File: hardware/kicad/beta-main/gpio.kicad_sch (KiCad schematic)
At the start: 1 part

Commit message: tweaks and added servo controller
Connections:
- net UART3_TX: now reaches Module1.39 (GPIO8)
- net UART3_RX: now reaches Module1.40 (GPIO9)
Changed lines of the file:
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@@
+	(wire
+		(pts
+			(xy 129.54 92.71) (xy 140.97 92.71)
+		)
+		(stroke
+			(width 0)
+			(type default)
+		)
+	)
 	(wire
 		(pts
@@
 		(pts
 			(xy 130.81 148.59) (xy 130.81 146.05)
+		)
+		(stroke
+			(width 0)
+			(type default)
+		)
+	)
+	(wire
+		(pts
+			(xy 57.15 92.71) (xy 68.58 92.71)
 		)
 		(stroke
@@
 		)
 	)
+	(hierarchical_label "UART3_TX"
+		(shape passive)
+		(at 140.97 92.71 0)
+		(effects
+			(font
+				(size 1.27 1.27)
+			)
+			(justify left)
+		)
+	)
 	(hierarchical_label "GND"
 		(shape passive)
@@
 		(effects
 			(font
+				(size 1.27 1.27)
+			)
+			(justify right)
+		)
+	)
+	(hierarchical_label "UART3_RX"
+		(shape passive)
+		(at 57.15 92.71 180)
+		(effects
+			(font

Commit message: tweaks
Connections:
- net CAM_GPIO1: now reaches Module1.100 (CAM_GPIO1)
- net CAM_GPIO0: now reaches Module1.97 (CAM_GPIO0)
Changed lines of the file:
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@@
+	(wire
+		(pts
+			(xy 62.23 168.91) (xy 68.58 168.91)
+		)
+		(stroke
+			(width 0)
+			(type default)
+		)
+	)
 	(wire
 		(pts
@@
 	(wire
 		(pts
+			(xy 129.54 166.37) (xy 134.62 166.37)
+		)
+		(stroke
+			(width 0)
+			(type default)
+		)
+	)
+	(wire
+		(pts
 			(xy 66.04 69.85) (xy 68.58 69.85)
 		)
@@
 		(shape passive)
 		(at 66.04 95.25 180)
+		(effects
+			(font
+				(size 1.27 1.27)
+			)
+			(justify right)
+		)
+	)
+	(hierarchical_label "SDA1"
+		(shape passive)
+		(at 22.86 128.27 180)
 		(effects
 			(font
@@
 		)
 	)
+	(hierarchical_label "CAM_GPIO0"
+		(shape input)
+		(at 134.62 166.37 0)
+		(effects
+			(font
+				(size 1.27 1.27)
+			)
+			(justify left)
+		)
+	)
 	(hierarchical_label "GND"
 		(shape passive)
@@
 		)
 	)
+	(hierarchical_label "SCL1"
+		(shape passive)
+		(at 22.86 124.46 180)
+		(effects
+			(font
+				(size 1.27 1.27)
+			)
+			(justify right)
+		)
+	)
 	(hierarchical_label "UART3_TX"
 		(shape passive)
@@
 		)
 	)
+	(hierarchical_label "CAM_GPIO1"
+		(shape input)
+		(at 62.23 168.91 180)
+		(effects
+			(font
+				(size 1.27 1.27)
+			)
+			(justify right)
+		)
+	)

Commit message: Wzmacniacz dodany
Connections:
- net GPIO21: now reaches Module1.25 (GPIO21)
- net GPIO19: now reaches Module1.26 (GPIO19)
- net GPIO18: now reaches Module1.49 (GPIO18)
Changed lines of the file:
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@@
+		)
+	)
+	(hierarchical_label "GPIO21"
+		(shape input)
+		(at 129.54 74.93 0)
+		(effects
+			(font
+				(size 1.27 1.27)
+			)
+			(justify left)
 		)
 	)
@@
 		(effects
 			(font
+				(size 1.27 1.27)
+			)
+			(justify left)
+		)
+	)
+	(hierarchical_label "GPIO19"
+		(shape input)
+		(at 68.58 74.93 180)
+		(effects
+			(font
+				(size 1.27 1.27)
+			)
+			(justify right)
+		)
+	)
+	(hierarchical_label "GPIO18"
+		(shape input)
+		(at 129.54 105.41 0)
+		(effects
+			(font

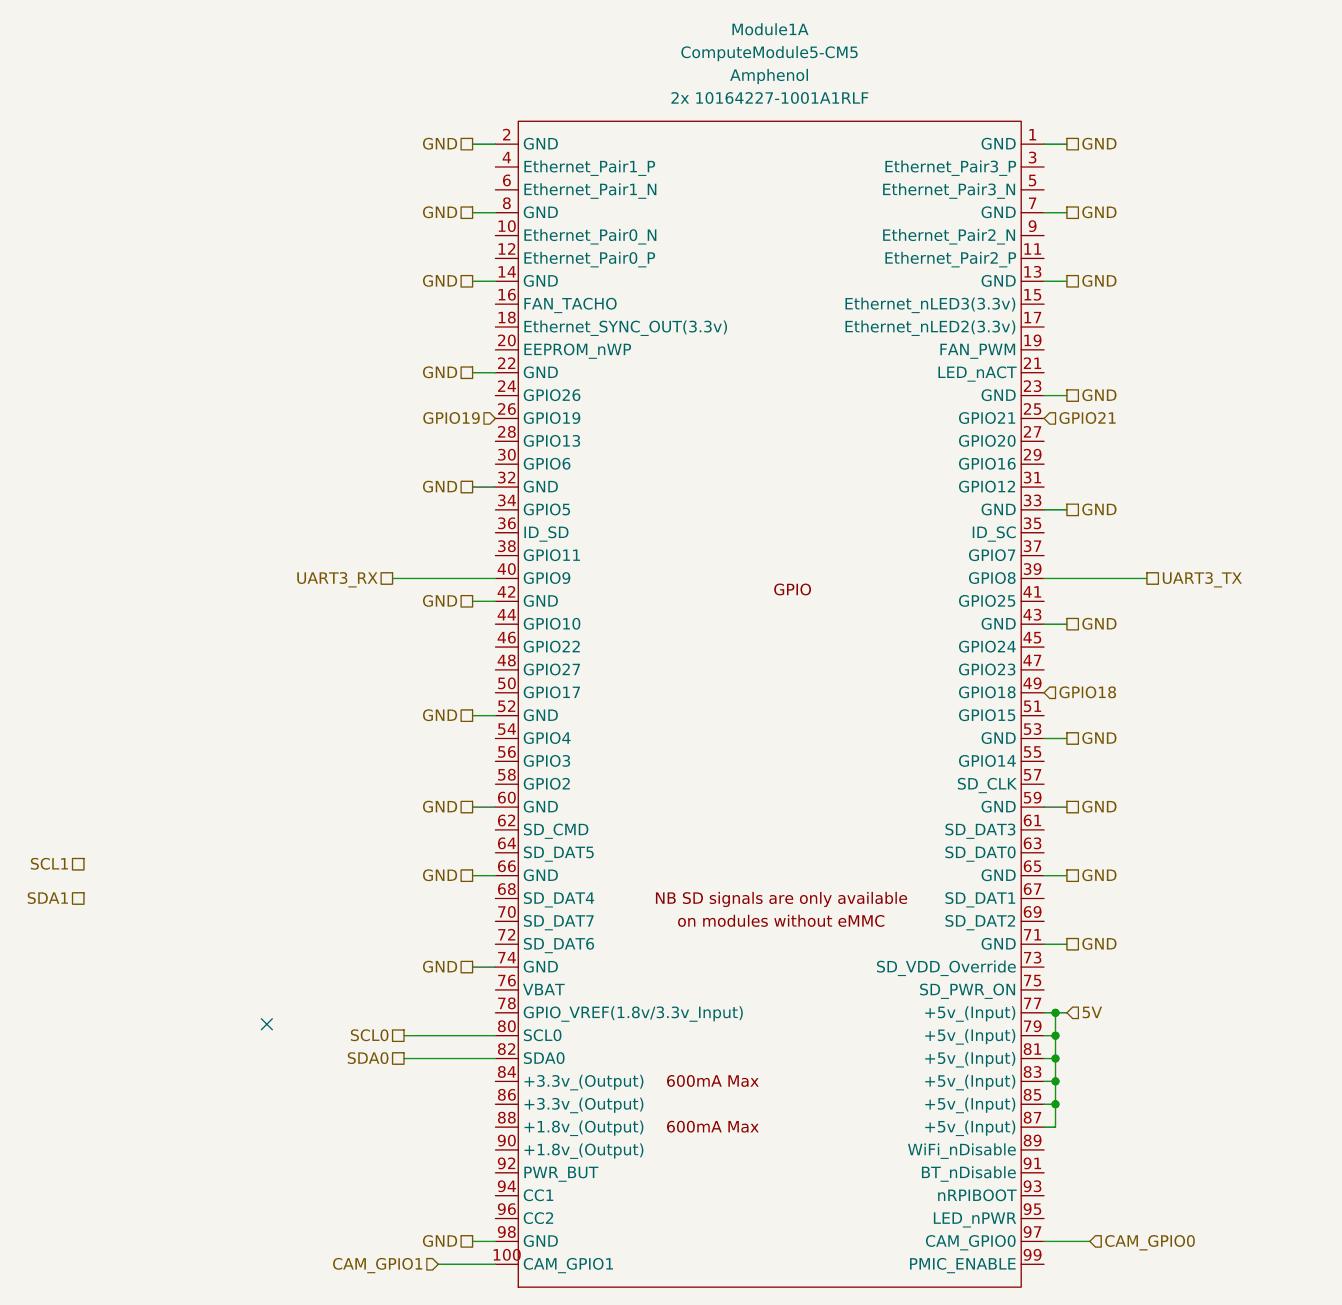
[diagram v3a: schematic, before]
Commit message: 5V and amplifier corrections
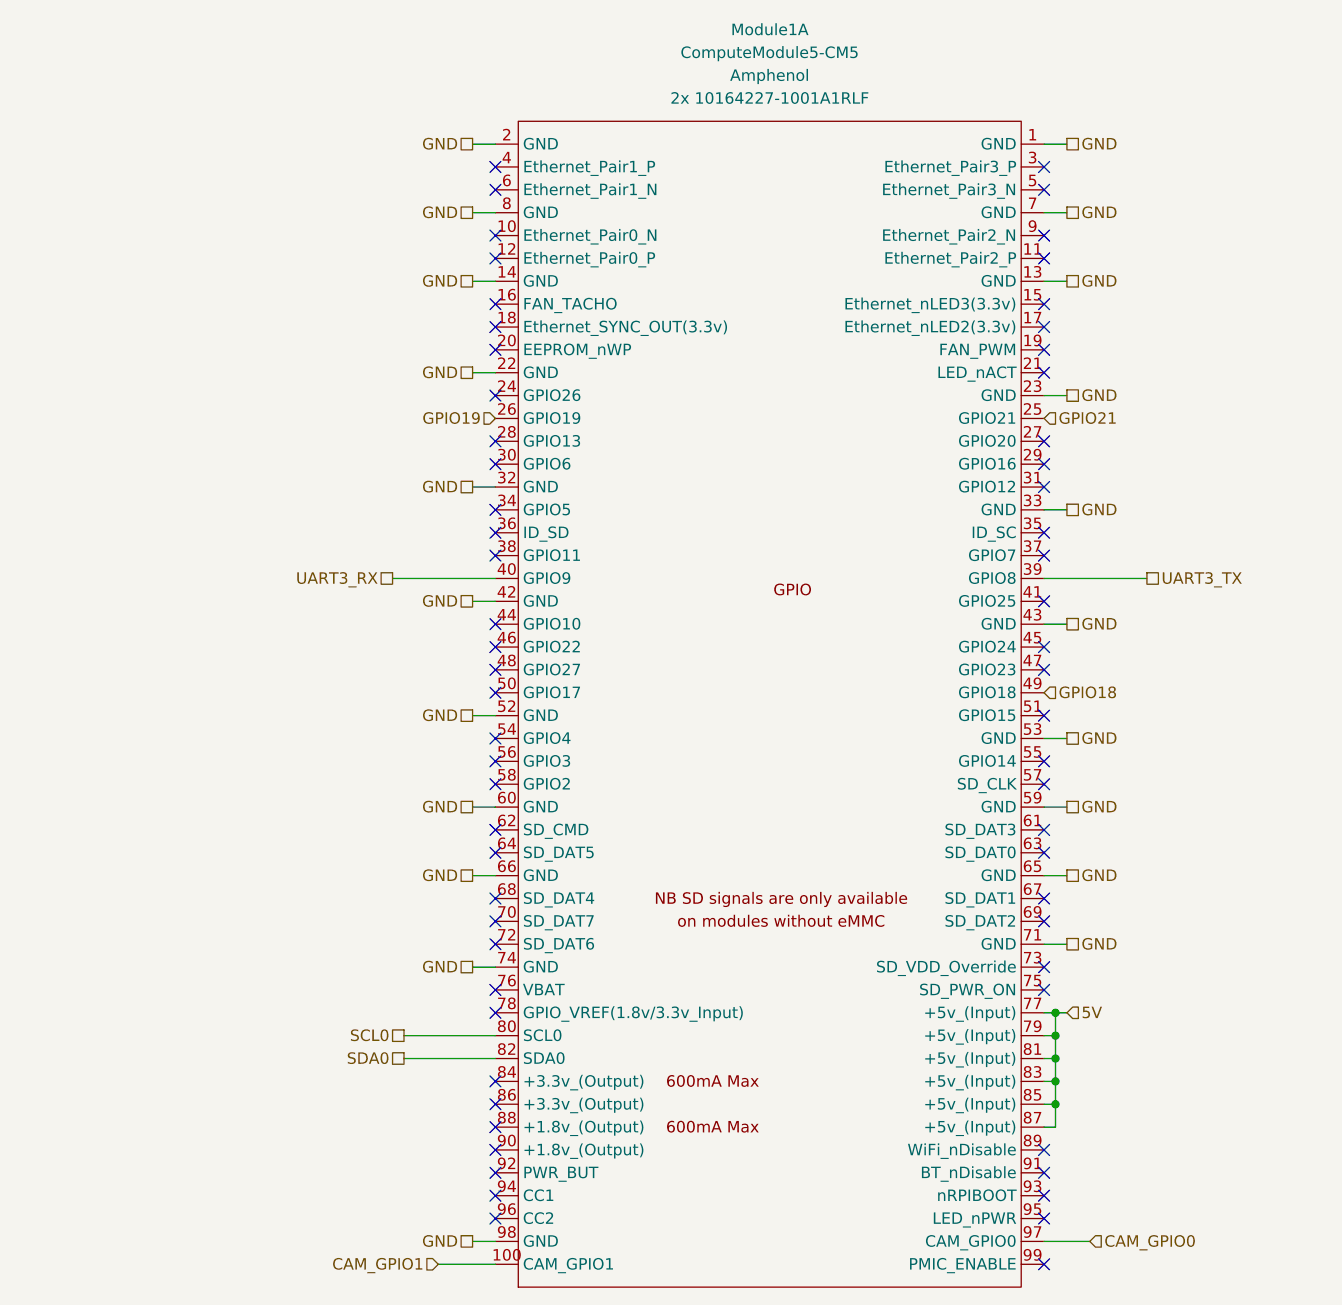
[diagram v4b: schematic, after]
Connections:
- no-connect marks 1 -> 64
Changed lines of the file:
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@@
 	)
 	(no_connect
-		(at 43.18 142.24)
+		(at 68.58 62.23)
+	)
+	(no_connect
+		(at 129.54 138.43)
+	)
+	(no_connect
+		(at 68.58 148.59)
+	)
+	(no_connect
+		(at 68.58 113.03)
+	)
+	(no_connect
+		(at 68.58 105.41)
+	)
+	(no_connect
+		(at 129.54 161.29)
+	)
+	(no_connect
+		(at 68.58 130.81)
+	)
+	(no_connect
+		(at 68.58 153.67)
+	)
+	(no_connect
+		(at 68.58 46.99)
+	)
+	(no_connect
+		(at 129.54 62.23)
+	)
+	(no_connect
+		(at 68.58 123.19)
+	)
+	(no_connect
+		(at 129.54 82.55)
+	)
+	(no_connect
+		(at 68.58 72.39)
+	)
+	(no_connect
+		(at 68.58 110.49)
+	)
+	(no_connect
+		(at 129.54 115.57)
+	)
+	(no_connect
+		(at 68.58 87.63)
+	)
+	(no_connect
+		(at 129.54 102.87)
+	)
+	(no_connect
+		(at 68.58 90.17)
+	)
+	(no_connect
+		(at 68.58 49.53)
+	)
+	(no_connect
+		(at 129.54 80.01)
+	)
+	(no_connect
+		(at 68.58 158.75)
+	)
+	(no_connect
+		(at 129.54 156.21)
+	)
+	(no_connect
+		(at 129.54 128.27)
+	)
+	(no_connect
+		(at 68.58 77.47)
+	)
+	(no_connect
+		(at 129.54 69.85)
+	)
+	(no_connect
+		(at 68.58 156.21)
+	)
+	(no_connect
+		(at 68.58 161.29)
+	)
+	(no_connect
+		(at 68.58 54.61)
+	)
+	(no_connect
+		(at 68.58 102.87)
+	)
+	(no_connect
+		(at 68.58 133.35)
+	)
+	(no_connect
+		(at 68.58 140.97)
+	)
+	(no_connect
+		(at 129.54 107.95)
+	)
+	(no_connect
+		(at 68.58 100.33)
+	)
+	(no_connect
+		(at 129.54 163.83)
+	)
+	(no_connect
+		(at 68.58 115.57)
+	)
+	(no_connect
+		(at 129.54 100.33)
+	)
+	(no_connect
+		(at 68.58 57.15)
+	)
+	(no_connect
+		(at 129.54 168.91)
+	)
+	(no_connect
+		(at 129.54 57.15)
+	)
+	(no_connect
+		(at 129.54 120.65)
+	)
+	(no_connect
+		(at 68.58 67.31)
+	)
+	(no_connect
+		(at 68.58 97.79)
+	)
+	(no_connect
+		(at 129.54 158.75)
+	)
+	(no_connect
+		(at 68.58 80.01)
+	)
+	(no_connect
+		(at 68.58 138.43)
+	)
+	(no_connect
+		(at 68.58 64.77)
+	)
+	(no_connect
+		(at 129.54 135.89)
+	)
+	(no_connect
+		(at 129.54 54.61)
+	)
+	(no_connect
+		(at 129.54 77.47)
+	)
+	(no_connect
+		(at 129.54 46.99)
+	)
+	(no_connect
+		(at 129.54 123.19)
+	)
+	(no_connect
+		(at 129.54 49.53)
+	)
+	(no_connect
+		(at 129.54 90.17)
+	)
+	(no_connect
+		(at 129.54 67.31)
+	)
+	(no_connect
+		(at 129.54 130.81)
+	)
+	(no_connect
+		(at 129.54 95.25)
+	)
+	(no_connect
+		(at 129.54 64.77)
+	)
+	(no_connect
+		(at 68.58 163.83)
+	)
+	(no_connect
+		(at 129.54 113.03)
+	)
+	(no_connect
+		(at 68.58 128.27)
+	)
+	(no_connect
+		(at 129.54 87.63)
+	)
+	(no_connect
+		(at 68.58 120.65)
+	)
+	(no_connect
+		(at 68.58 85.09)
+	)
+	(no_connect
+		(at 68.58 151.13)
 	)
 	(wire
@@
 		)
 	)
-	(hierarchical_label "SDA1"
-		(shape passive)
-		(at 22.86 128.27 180)
-		(effects
-			(font
-				(size 1.27 1.27)
-			)
-			(justify right)
-		)
-	)
 	(hierarchical_label "GND"
 		(shape passive)
@@
 		)
 	)
-	(hierarchical_label "SCL1"
-		(shape passive)
-		(at 22.86 124.46 180)
-		(effects
-			(font
-				(size 1.27 1.27)
-			)
-			(justify right)
-		)
-	)

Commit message: Amplifier set for left channel only and god rid of all errors from ERC
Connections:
- net SCL1: now reaches Module1.56 (GPIO3)
- net SDA1: now reaches Module1.58 (GPIO2)
- no-connect marks 64 -> 62
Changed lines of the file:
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@@
+	)
+	(junction
+		(at 133.35 140.97)
+		(diameter 0)
+		(color 0 0 0 0)
 	)
 	(junction
@@
 	)
 	(no_connect
-		(at 68.58 113.03)
-	)
-	(no_connect
 		(at 68.58 105.41)
 	)
@@
 	)
 	(no_connect
-		(at 68.58 115.57)
-	)
-	(no_connect
 		(at 129.54 100.33)
 	)
@@
 	(wire
 		(pts
-			(xy 130.81 140.97) (xy 132.08 140.97)
+			(xy 130.81 140.97) (xy 133.35 140.97)
 		)
 		(stroke
@@
 	(wire
 		(pts
+			(xy 133.35 140.97) (xy 134.62 140.97)
+		)
+		(stroke
+			(width 0)
+			(type default)
+		)
+	)
+	(wire
+		(pts
 			(xy 132.08 72.39) (xy 129.54 72.39)
 		)
@@
 	(wire
 		(pts
+			(xy 58.42 115.57) (xy 68.58 115.57)
+		)
+		(stroke
+			(width 0)
+			(type default)
+		)
+	)
+	(wire
+		(pts
 			(xy 132.08 44.45) (xy 129.54 44.45)
 		)
@@
 		(pts
 			(xy 129.54 151.13) (xy 130.81 151.13)
+		)
+		(stroke
+			(width 0)
+			(type default)
+		)
+	)
+	(wire
+		(pts
+			(xy 58.42 113.03) (xy 68.58 113.03)
 		)
 		(stroke
@@
 	(hierarchical_label "5V"
 		(shape input)
-		(at 132.08 140.97 0)
+		(at 134.62 140.97 0)
 		(effects
 			(font
@@
 		)
 	)
+	(hierarchical_label "SDA1"
+		(shape passive)
+		(at 58.42 115.57 180)
+		(effects
+			(font
+				(size 1.27 1.27)
+			)
+			(justify right)
+		)
+	)
 	(hierarchical_label "CAM_GPIO1"
 		(shape input)
 		(at 62.23 168.91 180)
+		(effects
+			(font
+				(size 1.27 1.27)
+			)
+			(justify right)
+		)
+	)
+	(hierarchical_label "SCL1"
+		(shape passive)
+		(at 58.42 113.03 180)
 		(effects
 			(font
@@
 					(unit 1)
 				)
+			)
+		)
+	)
+	(symbol
+		(lib_id "power:PWR_FLAG")
+		(at 133.35 140.97 0)
+		(unit 1)
+		(exclude_from_sim no)
+		(in_bom yes)
+		(on_board yes)
+		(dnp no)
+		(fields_autoplaced yes)
+		(property "Reference" "#FLG04"
+			(at 133.35 139.065 0)
+			(effects
+				(font
+					(size 1.27 1.27)
+				)
+				(hide yes)
+			)
+		)
+		(property "Value" "PWR_FLAG"
+			(at 133.35 135.89 0)
+			(effects
+				(font
+					(size 1.27 1.27)
+				)
+			)
+		)
+		(property "Footprint" ""
+			(at 133.35 140.97 0)
+			(effects
+				(font
+					(size 1.27 1.27)
+				)
+				(hide yes)
+			)
+		)
+		(property "Datasheet" "~"
+			(at 133.35 140.97 0)
+			(effects
+				(font
+					(size 1.27 1.27)
+				)
+				(hide yes)
+			)
+		)
+		(property "Description" "Special symbol for telling ERC where power comes from"
+			(at 133.35 140.97 0)
+			(effects
+				(font
+					(size 1.27 1.27)
+				)
+				(hide yes)
+			)
+		)
+		(pin "1"
+		)
+		(instances
+			(project "beta-main"
+				(path "/ec75fd42-4efa-4f32-b57e-76d632cb46f5/b3cf40a7-4d41-420e-a440-2c08f4160b31/2457c445-1c7f-4f98-9485-5d4e226b5b8f"
+					(reference "#FLG04")
+					(unit 1)
+				)

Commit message: Gyroscope added without errors in ERC
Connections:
- net SCL2: now reaches Module1.34 (GPIO5)
- net SDI: now reaches Module1.45 (GPIO24)
- net GPIO23: now reaches Module1.47 (GPIO23)
- net SDA2: now reaches Module1.54 (GPIO4)
- net GPIO18 renamed SCLK
- net GPIO19 renamed WS
- net GPIO21 renamed SDO
- no-connect marks 62 -> 58
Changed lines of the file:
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@@
-	)
-	(no_connect
-		(at 68.58 110.49)
 	)
 	(no_connect
@@
 	)
 	(no_connect
-		(at 129.54 102.87)
-	)
-	(no_connect
 		(at 68.58 90.17)
 	)
@@
 	)
 	(no_connect
-		(at 129.54 100.33)
-	)
-	(no_connect
 		(at 68.58 57.15)
 	)
@@
 	)
 	(no_connect
-		(at 68.58 85.09)
-	)
-	(no_connect
 		(at 68.58 151.13)
 	)
@@
 	(wire
 		(pts
+			(xy 129.54 100.33) (xy 132.08 100.33)
+		)
+		(stroke
+			(width 0)
+			(type default)
+		)
+	)
+	(wire
+		(pts
 			(xy 133.35 140.97) (xy 134.62 140.97)
 		)
@@
 	(wire
 		(pts
+			(xy 66.04 85.09) (xy 68.58 85.09)
+		)
+		(stroke
+			(width 0)
+			(type default)
+		)
+	)
+	(wire
+		(pts
 			(xy 132.08 85.09) (xy 129.54 85.09)
 		)
@@
 	(wire
 		(pts
+			(xy 132.08 105.41) (xy 129.54 105.41)
+		)
+		(stroke
+			(width 0)
+			(type default)
+		)
+	)
+	(wire
+		(pts
 			(xy 132.08 110.49) (xy 129.54 110.49)
 		)
@@
 	(wire
 		(pts
+			(xy 66.04 74.93) (xy 68.58 74.93)
+		)
+		(stroke
+			(width 0)
+			(type default)
+		)
+	)
+	(wire
+		(pts
+			(xy 132.08 74.93) (xy 129.54 74.93)
+		)
+		(stroke
+			(width 0)
+			(type default)
+		)
+	)
+	(wire
+		(pts
 			(xy 130.81 153.67) (xy 130.81 151.13)
 		)
@@
 	(wire
 		(pts
+			(xy 129.54 102.87) (xy 132.08 102.87)
+		)
+		(stroke
+			(width 0)
+			(type default)
+		)
+	)
+	(wire
+		(pts
 			(xy 132.08 97.79) (xy 129.54 97.79)
 		)
@@
 	(wire
 		(pts
+			(xy 58.42 110.49) (xy 68.58 110.49)
+		)
+		(stroke
+			(width 0)
+			(type default)
+		)
+	)
+	(wire
+		(pts
 			(xy 129.54 166.37) (xy 134.62 166.37)
 		)
@@
 		)
 	)
-	(hierarchical_label "GPIO21"
-		(shape input)
-		(at 129.54 74.93 0)
+	(hierarchical_label "SDO"
+		(shape passive)
+		(at 132.08 74.93 0)
 		(effects
 			(font
@@
 		)
 	)
-	(hierarchical_label "GPIO19"
-		(shape input)
-		(at 68.58 74.93 180)
-		(effects
-			(font
-				(size 1.27 1.27)
-			)
-			(justify right)
-		)
-	)
-	(hierarchical_label "GPIO18"
-		(shape input)
-		(at 129.54 105.41 0)
+	(hierarchical_label "GPIO23"
+		(shape passive)
+		(at 132.08 102.87 0)
+		(effects
+			(font
+				(size 1.27 1.27)
+			)
+			(justify left)
+		)
+	)
+	(hierarchical_label "WS"
+		(shape passive)
+		(at 66.04 74.93 180)
+		(effects
+			(font
+				(size 1.27 1.27)
+			)
+			(justify right)
+		)
+	)
+	(hierarchical_label "SCLK"
+		(shape passive)
+		(at 132.08 105.41 0)
 		(effects
 			(font
@@
 		)
 	)
+	(hierarchical_label "SCL2"
+		(shape passive)
+		(at 66.04 85.09 180)
+		(effects
+			(font
+				(size 1.27 1.27)
+			)
+			(justify right)
+		)
+	)
 	(hierarchical_label "GND"
 		(shape passive)
@@
 			)
 			(justify left)
+		)
+	)
+	(hierarchical_label "SDA2"
+		(shape passive)
+		(at 58.42 110.49 180)
+		(effects
+			(font
+				(size 1.27 1.27)
+			)
+			(justify right)
 		)
 	)
@@
 	)
 	(hierarchical_label "CAM_GPIO0"
-		(shape input)
+		(shape passive)
 		(at 134.62 166.37 0)
 		(effects
@@
 		)
 	)
+	(hierarchical_label "SDI"
+		(shape passive)
+		(at 132.08 100.33 0)
+		(effects
+			(font
+				(size 1.27 1.27)
+			)
+			(justify left)
+		)
+	)
 	(hierarchical_label "GND"
 		(shape passive)
@@
 	)
 	(hierarchical_label "CAM_GPIO1"
-		(shape input)
+		(shape passive)
 		(at 62.23 168.91 180)
 		(effects
